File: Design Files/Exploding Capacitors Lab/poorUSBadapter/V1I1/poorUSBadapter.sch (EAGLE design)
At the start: 0 parts

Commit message: Schematic update
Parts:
- added D1, D2: (no value), diode:ZENER-DIODESOD80C
- added R1: 1k5, SparkFun-Passives:RESISTOR0805-RES
- added R2: 1M, SparkFun-Passives:RESISTOR0805-RES
- added R3, R4: 68R, SparkFun-Passives:RESISTOR0805-RES
- added S1: SWITCH-MOMENTARY-2SMD-1101NE, SparkFun-Electromechanical:SWITCH-MOMENTARY-2SMD-1101NE
- added USB1: CON-USB-F-MINI-B, dp_devices:CON-USB-F-MINI-B
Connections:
- new net GND: D1.A, D2.A, R2.1, S1.1, USB1USB.GND
- new net N$1: D1.C, R2.2, R4.1, USB1USB.D+
- new net N$2: D2.C, R1.1, R3.1, USB1USB.D-
- new net N$5: R3.2
- new net N$6: R4.2
- new net VCC: R1.2

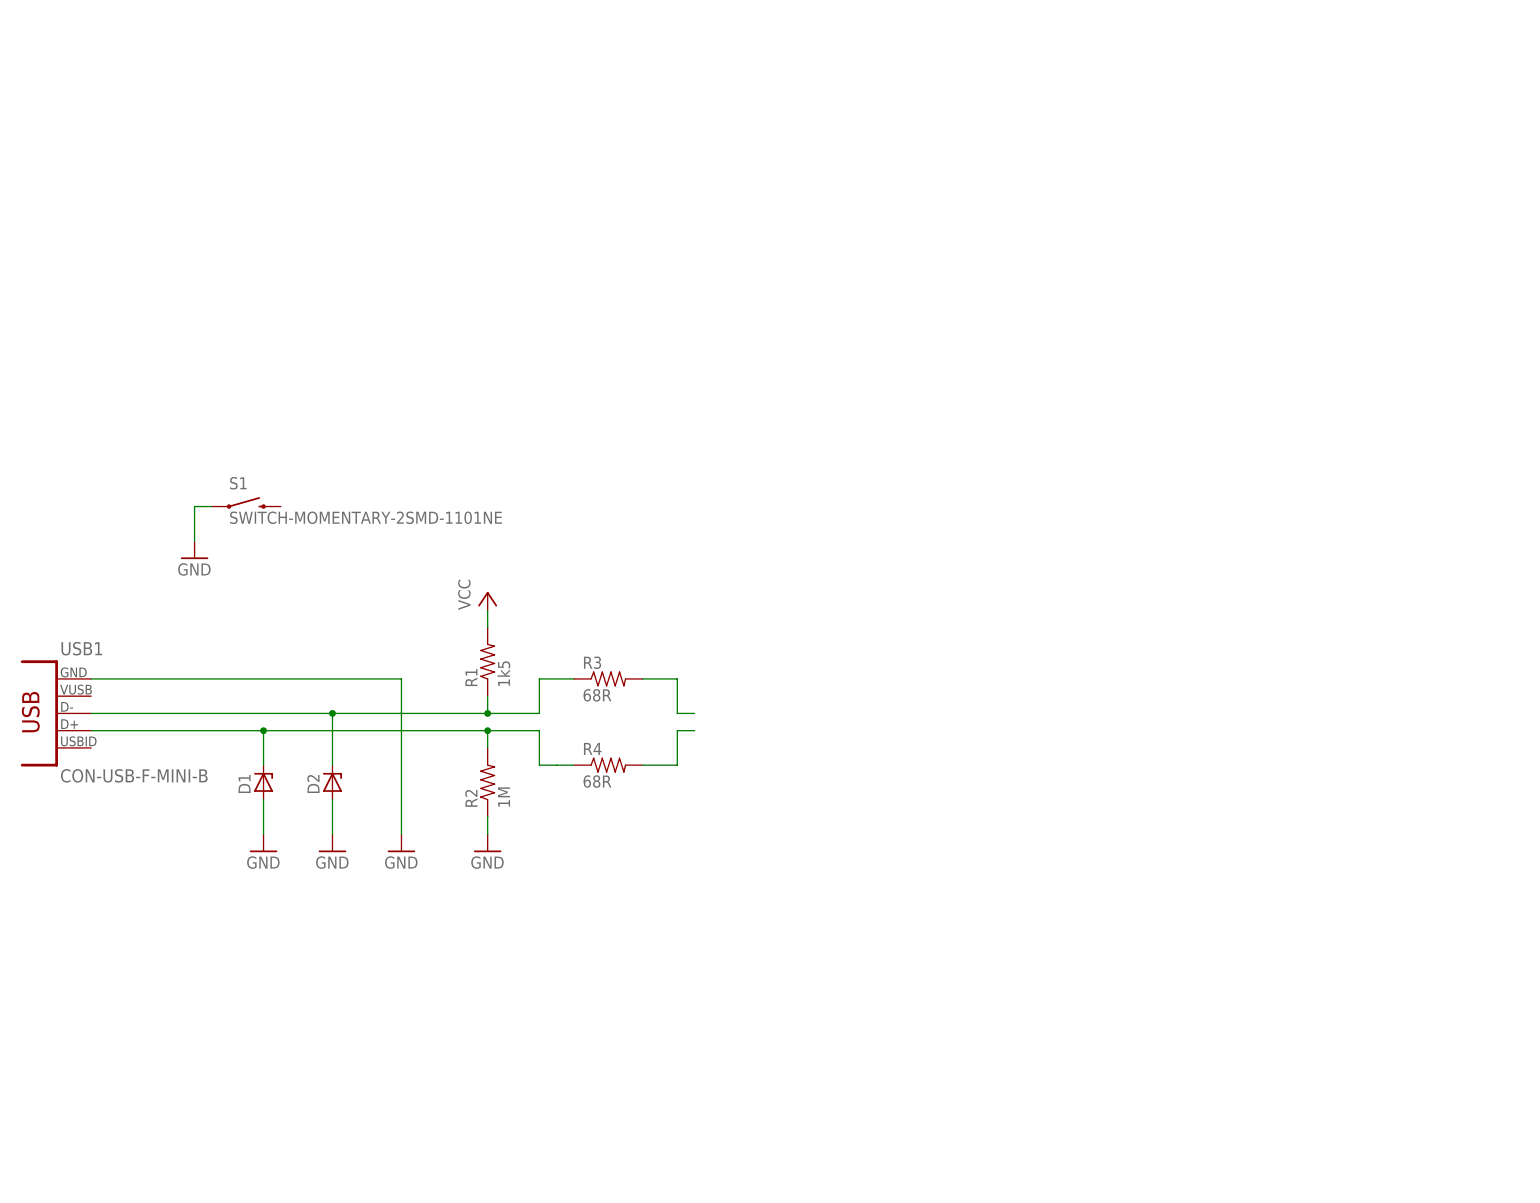
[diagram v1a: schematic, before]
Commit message: Zener diodes changed to microMELF, fixed connector size
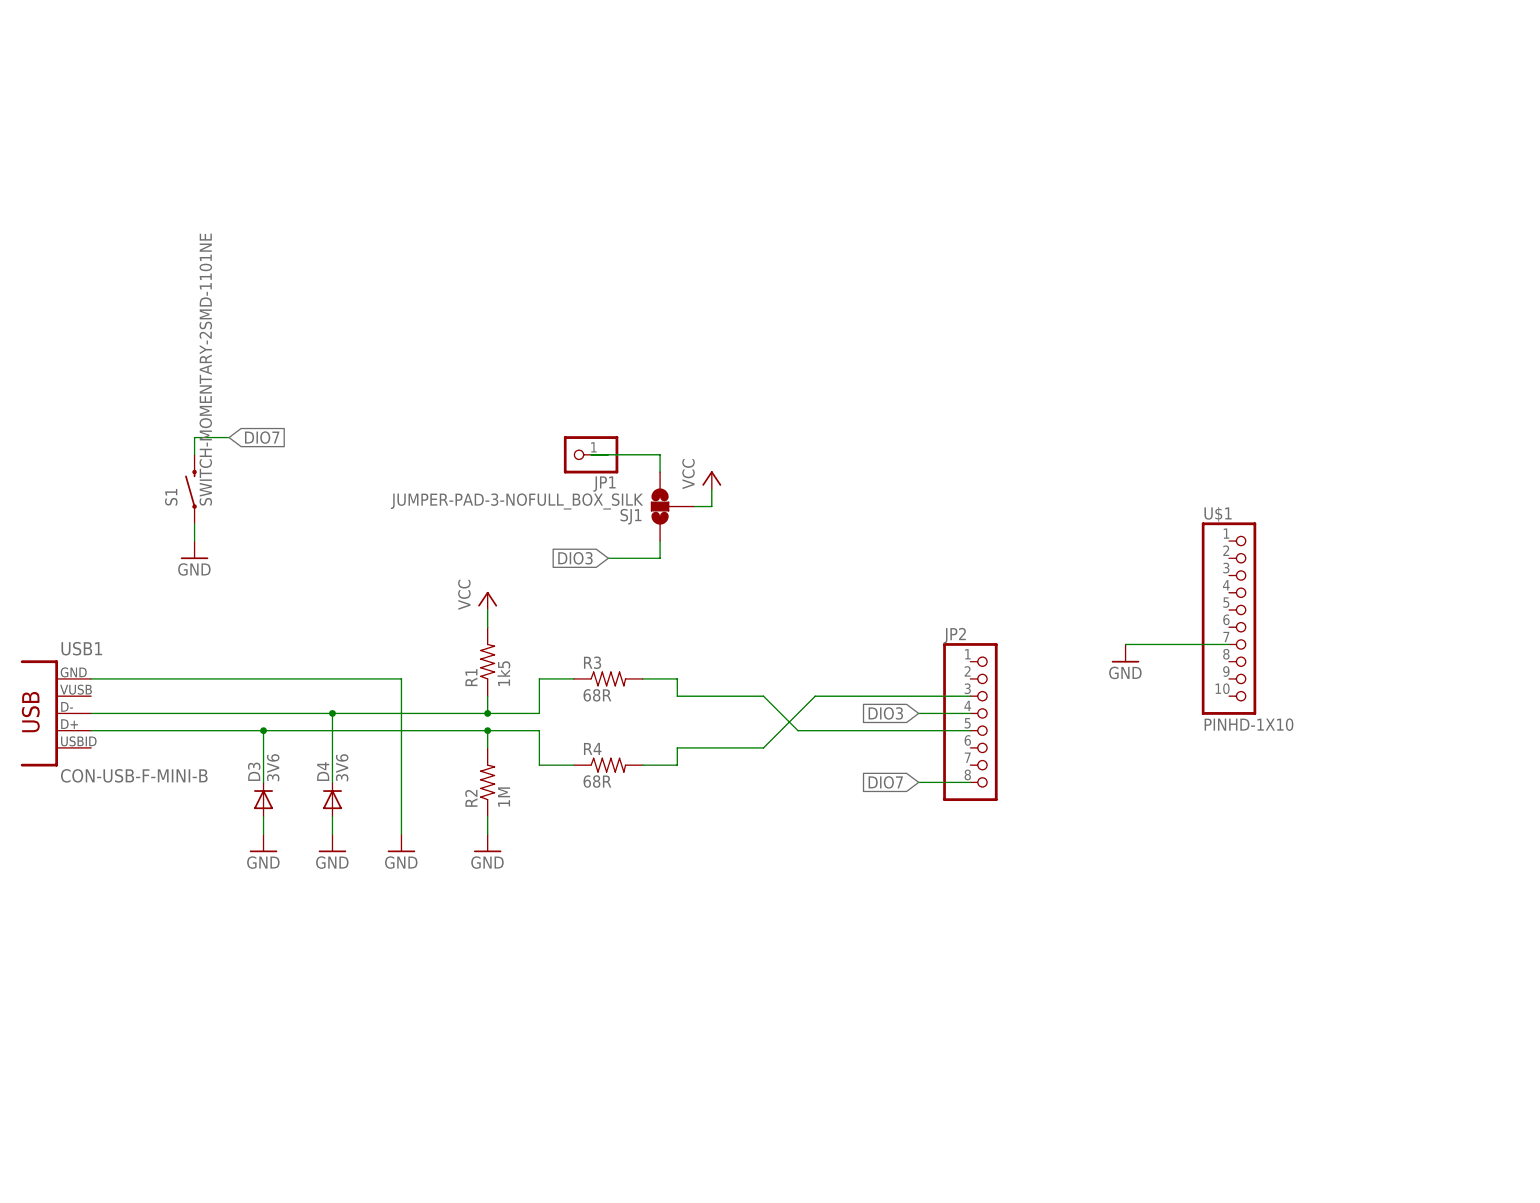
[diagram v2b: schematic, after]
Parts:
- removed D1, D2: (no value), diode:ZENER-DIODESOD80C
- added D3, D4: 3V6, diode:DIODE-MICROMELF-W
- added JP1: (no value), adafruit:PINHD-1X1
- added JP2: (no value), adafruit:PINHD-1X8BIG
- added SJ1: JUMPER-PAD-3-NOFULL_BOX_SILK, SparkFun-Passives:JUMPER-PAD-3-NOFULL_BOX_SILK
- added U$1: PINHD-1X10, adafruit:PINHD-1X10
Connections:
- removed net N$1: D1.C, R2.2, R4.1, USB1USB.D+
- removed net N$2: D2.C, R1.1, R3.1, USB1USB.D-
- removed net N$5: R3.2
- removed net N$6: R4.2
- new net DIO3: JP2.4, SJ1.1
- new net DIO7: JP2.8, S1.2
- new net N$3: JP1.1, SJ1.3
- new net USB_N: D4.C, R1.1, R3.1, USB1USB.D-
- new net USB_P: D3.C, R2.2, R4.1, USB1USB.D+
- new net U_N: JP2.5, R3.2
- new net U_P: JP2.3, R4.2
- net GND: now also D3.A, D4.A, U$1.7; no longer D1.A, D2.A
- net VCC: now also SJ1.2
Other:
- moved on the sheet: S1
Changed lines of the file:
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@@
 <parts>
 <part name="FRAME1" library="frames" deviceset="A4L-LOC" device=""/>
-<part name="D1" library="diode" deviceset="ZENER-DIODE" device="SOD80C"/>
-<part name="D2" library="diode" deviceset="ZENER-DIODE" device="SOD80C"/>
 <part name="GND1" library="supply1" deviceset="GND" device=""/>
 <part name="P+1" library="supply1" deviceset="VCC" device=""/>
@@
 <part name="S1" library="SparkFun-Electromechanical" deviceset="SWITCH-MOMENTARY-2" device="SMD-1101NE"/>
 <part name="GND5" library="supply1" deviceset="GND" device=""/>
+<part name="SJ1" library="SparkFun-Passives" deviceset="JUMPER-PAD-3-NO" device="FULL_BOX_SILK"/>
+<part name="P+2" library="supply1" deviceset="VCC" device=""/>
+<part name="JP1" library="adafruit" deviceset="PINHD-1X1" device=""/>
+<part name="D3" library="diode" deviceset="DIODE-" device="MICROMELF-W" value="3V6"/>
+<part name="D4" library="diode" deviceset="DIODE-" device="MICROMELF-W" value="3V6"/>
+<part name="U$1" library="adafruit" deviceset="PINHD-1X10" device=""/>
+<part name="JP2" library="adafruit" deviceset="PINHD-1X8" device="BIG"/>
+<part name="GND6" library="supply1" deviceset="GND" device=""/>
 </parts>
 <sheets>
@@
 <instances>
 <instance part="FRAME1" gate="G$1" x="0" y="0"/>
-<instance part="D1" gate="G$1" x="73.66" y="66.04" rot="R90"/>
-<instance part="D2" gate="G$1" x="83.82" y="66.04" rot="R90"/>
 <instance part="GND1" gate="1" x="93.98" y="55.88"/>
 <instance part="P+1" gate="VCC" x="106.68" y="93.98"/>
@@
 <instance part="R4" gate="G$1" x="124.46" y="68.58"/>
 <instance part="GND4" gate="1" x="106.68" y="55.88"/>
-<instance part="S1" gate="G$1" x="71.12" y="106.68"/>
+<instance part="S1" gate="G$1" x="63.5" y="109.22" rot="R90"/>
 <instance part="GND5" gate="1" x="63.5" y="99.06"/>
+<instance part="SJ1" gate="G$1" x="132.08" y="106.68" rot="R180"/>
+<instance part="P+2" gate="VCC" x="139.7" y="111.76"/>
+<instance part="JP1" gate="G$1" x="119.38" y="114.3" rot="R180"/>
+<instance part="D3" gate="G$1" x="73.66" y="63.5" rot="R90"/>
+<instance part="D4" gate="G$1" x="83.82" y="63.5" rot="R90"/>
+<instance part="U$1" gate="G$1" x="218.44" y="91.44"/>
+<instance part="JP2" gate="G$1" x="180.34" y="76.2"/>
+<instance part="GND6" gate="1" x="200.66" y="83.82"/>
 </instances>
 <busses>
 </busses>
 <nets>
-<net name="N$1" class="0">
+<net name="USB_P" class="0">
 <segment>
 <pinref part="USB1" gate="USB" pin="D+"/>
-<pinref part="D1" gate="G$1" pin="C"/>
 <wire x1="48.26" y1="73.66" x2="73.66" y2="73.66" width="0.1524" layer="91"/>
-<wire x1="73.66" y1="73.66" x2="73.66" y2="68.58" width="0.1524" layer="91"/>
+<wire x1="73.66" y1="73.66" x2="73.66" y2="66.04" width="0.1524" layer="91"/>
 <wire x1="73.66" y1="73.66" x2="106.68" y2="73.66" width="0.1524" layer="91"/>
 <junction x="73.66" y="73.66"/>
@@
 <wire x1="106.68" y1="73.66" x2="114.3" y2="73.66" width="0.1524" layer="91"/>
 <wire x1="114.3" y1="73.66" x2="114.3" y2="68.58" width="0.1524" layer="91"/>
-<wire x1="114.3" y1="68.58" x2="116.84" y2="68.58" width="0.1524" layer="91"/>
-<wire x1="116.84" y1="68.58" x2="119.38" y2="68.58" width="0.1524" layer="91"/>
+<wire x1="114.3" y1="68.58" x2="119.38" y2="68.58" width="0.1524" layer="91"/>
 <junction x="106.68" y="73.66"/>
+<pinref part="D3" gate="G$1" pin="C"/>
 </segment>
 </net>
-<net name="N$2" class="0">
+<net name="USB_N" class="0">
 <segment>
 <pinref part="USB1" gate="USB" pin="D-"/>
-<pinref part="D2" gate="G$1" pin="C"/>
 <wire x1="48.26" y1="76.2" x2="83.82" y2="76.2" width="0.1524" layer="91"/>
-<wire x1="83.82" y1="76.2" x2="83.82" y2="68.58" width="0.1524" layer="91"/>
+<wire x1="83.82" y1="76.2" x2="83.82" y2="66.04" width="0.1524" layer="91"/>
 <wire x1="83.82" y1="76.2" x2="106.68" y2="76.2" width="0.1524" layer="91"/>
 <junction x="83.82" y="76.2"/>
@@
 <wire x1="114.3" y1="81.28" x2="119.38" y2="81.28" width="0.1524" layer="91"/>
 <junction x="106.68" y="76.2"/>
+<pinref part="D4" gate="G$1" pin="C"/>
 </segment>
 </net>
 <net name="GND" class="0">
-<segment>
-<pinref part="D1" gate="G$1" pin="A"/>
-<wire x1="73.66" y1="63.5" x2="73.66" y2="58.42" width="0.1524" layer="91"/>
-<pinref part="GND2" gate="1" pin="GND"/>
-</segment>
-<segment>
-<pinref part="D2" gate="G$1" pin="A"/>
-<wire x1="83.82" y1="63.5" x2="83.82" y2="58.42" width="0.1524" layer="91"/>
-<pinref part="GND3" gate="1" pin="GND"/>
-</segment>
 <segment>
 <pinref part="GND1" gate="1" pin="GND"/>
@@
 <segment>
 <pinref part="S1" gate="G$1" pin="1"/>
-<wire x1="66.04" y1="106.68" x2="63.5" y2="106.68" width="0.1524" layer="91"/>
-<wire x1="63.5" y1="106.68" x2="63.5" y2="101.6" width="0.1524" layer="91"/>
+<wire x1="63.5" y1="104.14" x2="63.5" y2="101.6" width="0.1524" layer="91"/>
 <pinref part="GND5" gate="1" pin="GND"/>
+</segment>
+<segment>
+<pinref part="U$1" gate="G$1" pin="7"/>
+<pinref part="GND6" gate="1" pin="GND"/>
+<wire x1="215.9" y1="86.36" x2="200.66" y2="86.36" width="0.1524" layer="91"/>
+</segment>
+<segment>
+<pinref part="D3" gate="G$1" pin="A"/>
+<pinref part="GND2" gate="1" pin="GND"/>
+<wire x1="73.66" y1="60.96" x2="73.66" y2="58.42" width="0.1524" layer="91"/>
+</segment>
+<segment>
+<pinref part="D4" gate="G$1" pin="A"/>
+<pinref part="GND3" gate="1" pin="GND"/>
+<wire x1="83.82" y1="60.96" x2="83.82" y2="58.42" width="0.1524" layer="91"/>
 </segment>
 </net>
@@
 <pinref part="P+1" gate="VCC" pin="VCC"/>
 </segment>
+<segment>
+<pinref part="SJ1" gate="G$1" pin="2"/>
+<wire x1="137.16" y1="106.68" x2="139.7" y2="106.68" width="0.1524" layer="91"/>
+<wire x1="139.7" y1="106.68" x2="139.7" y2="109.22" width="0.1524" layer="91"/>
+<pinref part="P+2" gate="VCC" pin="VCC"/>
+</segment>
 </net>
-<net name="N$5" class="0">
+<net name="U_N" class="0">
 <segment>
+<pinref part="JP2" gate="G$1" pin="5"/>
+<wire x1="177.8" y1="73.66" x2="152.4" y2="73.66" width="0.1524" layer="91"/>
+<wire x1="152.4" y1="73.66" x2="147.32" y2="78.74" width="0.1524" layer="91"/>
 <pinref part="R3" gate="G$1" pin="2"/>
 <wire x1="129.54" y1="81.28" x2="134.62" y2="81.28" width="0.1524" layer="91"/>
-<wire x1="134.62" y1="81.28" x2="134.62" y2="76.2" width="0.1524" layer="91"/>
-<wire x1="134.62" y1="76.2" x2="137.16" y2="76.2" width="0.1524" layer="91"/>
+<wire x1="134.62" y1="81.28" x2="134.62" y2="78.74" width="0.1524" layer="91"/>
+<wire x1="147.32" y1="78.74" x2="134.62" y2="78.74" width="0.1524" layer="91"/>
 </segment>
 </net>
-<net name="N$6" class="0">
+<net name="U_P" class="0">
 <segment>
+<pinref part="JP2" gate="G$1" pin="3"/>
+<wire x1="177.8" y1="78.74" x2="154.94" y2="78.74" width="0.1524" layer="91"/>
+<wire x1="154.94" y1="78.74" x2="147.32" y2="71.12" width="0.1524" layer="91"/>
 <pinref part="R4" gate="G$1" pin="2"/>
 <wire x1="129.54" y1="68.58" x2="134.62" y2="68.58" width="0.1524" layer="91"/>
-<wire x1="134.62" y1="68.58" x2="134.62" y2="73.66" width="0.1524" layer="91"/>
-<wire x1="134.62" y1="73.66" x2="137.16" y2="73.66" width="0.1524" layer="91"/>
+<wire x1="134.62" y1="68.58" x2="134.62" y2="71.12" width="0.1524" layer="91"/>
+<wire x1="147.32" y1="71.12" x2="134.62" y2="71.12" width="0.1524" layer="91"/>
 </segment>
 </net>
+<net name="DIO7" class="0">
+<segment>
+<pinref part="S1" gate="G$1" pin="2"/>
+<wire x1="63.5" y1="114.3" x2="63.5" y2="116.84" width="0.1524" layer="91"/>
+<wire x1="63.5" y1="116.84" x2="68.58" y2="116.84" width="0.1524" layer="91"/>
+<label x="68.58" y="116.84" size="1.778" layer="95" xref="yes"/>
+</segment>
+<segment>
+<pinref part="JP2" gate="G$1" pin="8"/>
+<wire x1="177.8" y1="66.04" x2="170.18" y2="66.04" width="0.1524" layer="91"/>
+<label x="170.18" y="66.04" size="1.778" layer="95" rot="R180" xref="yes"/>
+</segment>
+</net>
+<net name="N$3" class="0">
+<segment>
+<pinref part="SJ1" gate="G$1" pin="3"/>
+<wire x1="132.08" y1="111.76" x2="132.08" y2="114.3" width="0.1524" layer="91"/>
+<wire x1="132.08" y1="114.3" x2="121.92" y2="114.3" width="0.1524" layer="91"/>
+<pinref part="JP1" gate="G$1" pin="1"/>
+<wire x1="121.92" y1="114.3" x2="124.46" y2="114.3" width="0.1524" layer="91"/>
+</segment>
+</net>
+<net name="DIO3" class="0">
+<segment>
+<pinref part="SJ1" gate="G$1" pin="1"/>
+<wire x1="132.08" y1="101.6" x2="132.08" y2="99.06" width="0.1524" layer="91"/>
+<wire x1="132.08" y1="99.06" x2="124.46" y2="99.06" width="0.1524" layer="91"/>
+<label x="124.46" y="99.06" size="1.778" layer="95" rot="R180" xref="yes"/>
+</segment>
+<segment>
+<pinref part="JP2" gate="G$1" pin="4"/>
+<wire x1="177.8" y1="76.2" x2="170.18" y2="76.2" width="0.1524" layer="91"/>
+<label x="170.18" y="76.2" size="1.778" layer="95" rot="R180" xref="yes"/>
+</segment>
+</net>
